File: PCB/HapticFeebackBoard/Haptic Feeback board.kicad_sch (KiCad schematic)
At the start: 3 parts, among them J1 Conn_01x02, J2 Conn_01x04, Q1 2N7002E

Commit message: Updated Haptic Feedback Board
Should be close to final schematic
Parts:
- removed J1: Conn_01x02, symbol Connector_Generic:Conn_01x02
- removed J2: Conn_01x04, symbol Connector_Generic:Conn_01x04
- added C1: 1uF, Capacitor_SMD:C_0805_2012Metric_Pad1.18x1.45mm_HandSolder, symbol Device:C_Small
- added H1, H2, H3, H4: MountingHole, MountingHole:MountingHole_3.2mm_M3, symbol Mechanical:MountingHole
- added J1: 1769, Adafruit Accessories JST-PH 2-pin SMT Right Angle Connect:1769, symbol 1769:1769
- added J2, J3, J4: Conn_01x02, Connector_Molex:Molex_KK-254_AE-6410-02A_1x02_P2.54mm_Vertical, symbol Connector_Generic:Conn_01x02
- added R1: 10k, Resistor_SMD:R_0805_2012Metric_Pad1.20x1.40mm_HandSolder, symbol Device:R
- added SW1: PTS526 SM15 SMTR2 LFS, PTS526 SM15 SMTR2 LFS:SON4_PTS526 SM15 SMTR2 LFS_CNK, symbol PTS526 SM15 SMTR2 LFS:PTS526_SM15_SMTR2_LFS
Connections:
- net BMS Power: now also J1.1, SW1.1, SW1.2
- net GND: now also C1.2, J1.2, J3.2 (Pin_2), J4.2 (Pin_2)
- net GPIO: now also Q1.1 (G), J2.2 (Pin_2)
- net Motor1: now reaches Q1.2 (S)
- net Motor1: now also J3.1 (Pin_1), J4.1 (Pin_1)
- new net: C1.1, R1.1, SW1.3, SW1.4
- new net MCU: J2.1 (Pin_1), R1.2

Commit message: Recovery attempt 2
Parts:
- removed C1: 1uF, Capacitor_SMD:C_0805_2012Metric_Pad1.18x1.45mm_HandSolder, symbol Device:C_Small
- removed H1, H2, H3, H4: MountingHole, MountingHole:MountingHole_3.2mm_M3, symbol Mechanical:MountingHole
- removed J1: 1769, Adafruit Accessories JST-PH 2-pin SMT Right Angle Connect:1769, symbol 1769:1769
- removed J2, J3, J4: Conn_01x02, Connector_Molex:Molex_KK-254_AE-6410-02A_1x02_P2.54mm_Vertical, symbol Connector_Generic:Conn_01x02
- removed R1: 10k, Resistor_SMD:R_0805_2012Metric_Pad1.20x1.40mm_HandSolder, symbol Device:R
- removed SW1: PTS526 SM15 SMTR2 LFS, PTS526 SM15 SMTR2 LFS:SON4_PTS526 SM15 SMTR2 LFS_CNK, symbol PTS526 SM15 SMTR2 LFS:PTS526_SM15_SMTR2_LFS
- added J1: Conn_01x02, symbol Connector_Generic:Conn_01x02
- added J2: Conn_01x04, symbol Connector_Generic:Conn_01x04
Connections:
- net BMS Power: now also J1.2 (Pin_2)
- net GND: now also J2.1 (Pin_1), J2.3 (Pin_3)
- net GPIO: no longer Q1.1 (G)
- net Motor1: no longer names the net of Q1.2 (S)
- net Motor1: now also J2.2 (Pin_2), J2.4 (Pin_4)
- new net: J1.1 (Pin_1), Q1.1 (G)
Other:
- company: (none) -> Running Cadence Measurement Belt
- title: (none) -> Haptic Feedback Board

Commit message: Updating Haptic Feedback Board
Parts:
- removed J1: Conn_01x02, symbol Connector_Generic:Conn_01x02
- removed J2: Conn_01x04, symbol Connector_Generic:Conn_01x04
- added C1: 1uF, Capacitor_SMD:C_0805_2012Metric_Pad1.18x1.45mm_HandSolder, symbol Device:C_Small
- added H1, H2, H3, H4: MountingHole, MountingHole:MountingHole_3.2mm_M3, symbol Mechanical:MountingHole
- added J1: 1769, Adafruit Accessories JST-PH 2-pin SMT Right Angle Connect:1769, symbol 1769:1769
- added J2, J3, J4: Conn_01x02, Connector_Molex:Molex_KK-254_AE-6410-02A_1x02_P2.54mm_Vertical, symbol Connector_Generic:Conn_01x02
- added R1: 10k, Resistor_SMD:R_0805_2012Metric_Pad1.20x1.40mm_HandSolder, symbol Device:R
- added SW1: PTS526 SM15 SMTR2 LFS, PTS526 SM15 SMTR2 LFS:SON4_PTS526 SM15 SMTR2 LFS_CNK, symbol PTS526 SM15 SMTR2 LFS:PTS526_SM15_SMTR2_LFS
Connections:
- net BMS Power: now also J1.1, SW1.1, SW1.2
- net GND: now also C1.2, J1.2, J3.2 (Pin_2), J4.2 (Pin_2)
- net GPIO: now also Q1.1 (G), J2.2 (Pin_2)
- net Motor1: now reaches Q1.2 (S)
- net Motor1: now also J3.1 (Pin_1), J4.1 (Pin_1)
- new net: C1.1, R1.1, SW1.3, SW1.4
- new net MCU: J2.1 (Pin_1), R1.2
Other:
- company: Running Cadence Measurement Belt -> (none)
- title: Haptic Feedback Board -> (none)

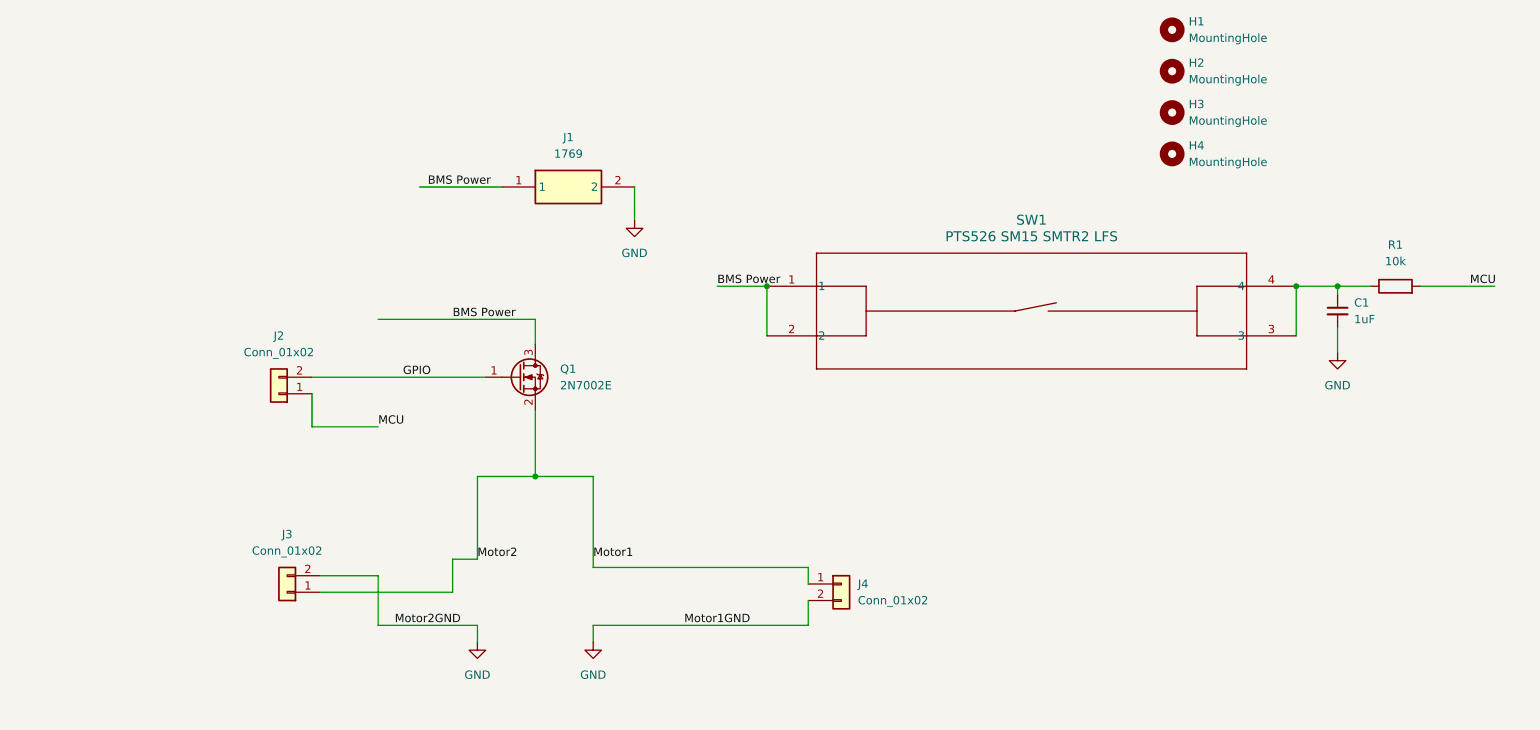
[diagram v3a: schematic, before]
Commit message: Further minor edits, added power LED
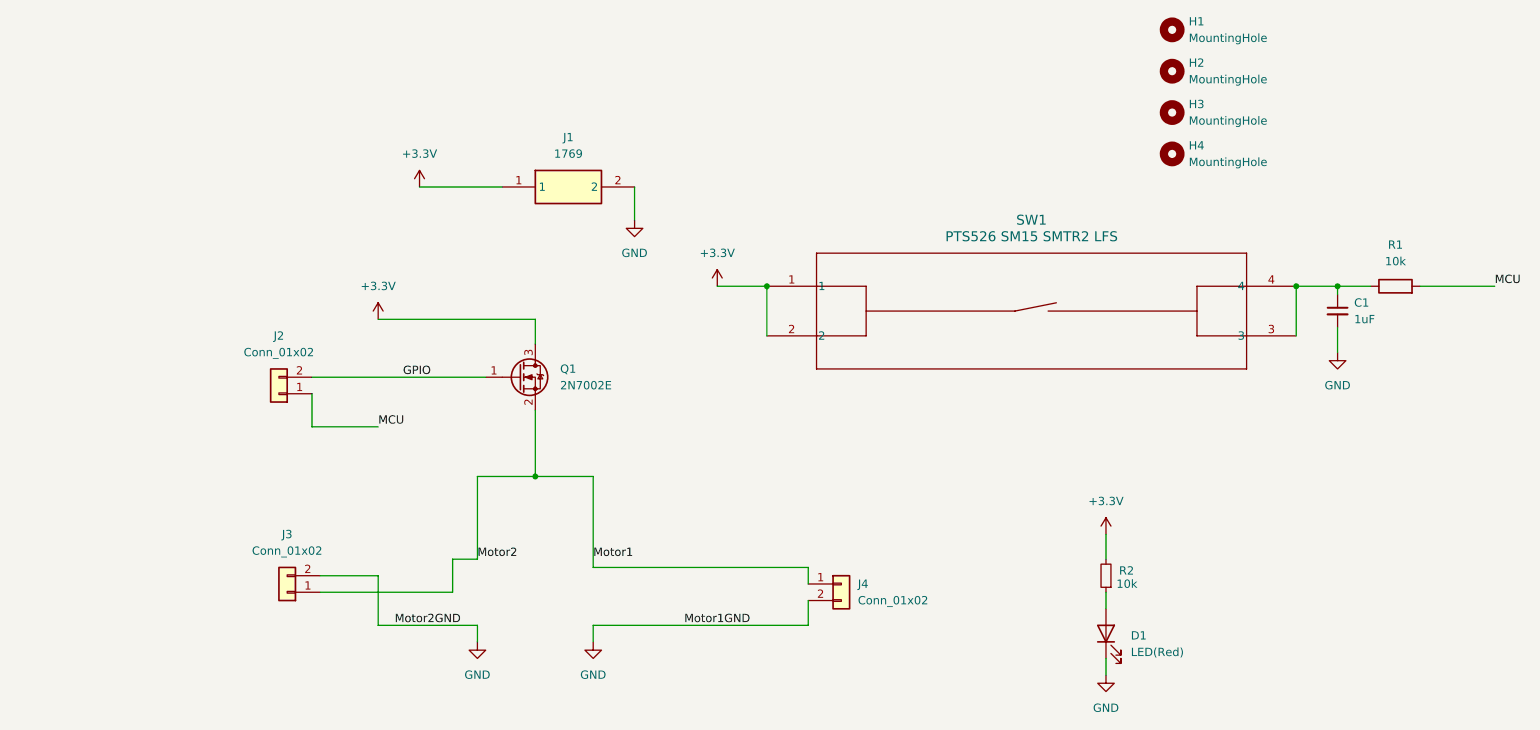
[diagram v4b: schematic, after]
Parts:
- added D1: LED(Red), LED_SMD:LED_0603_1608Metric_Pad1.05x0.95mm_HandSolder, symbol Device:LED
- added R2: 10k, Resistor_SMD:R_0805_2012Metric_Pad1.20x1.40mm_HandSolder, symbol Device:R_Small
- Q1: footprint Package_TO_SOT_SMD:SOT-23 -> Package_TO_SOT_SMD:SOT-23-3
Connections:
- net GND: now also D1.1 (K)
- net BMS Power renamed +3.3V
- net +3.3V: now also R2.2
- new net: D1.2 (A), R2.1

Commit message: Updated Haptic Feedback Board
Changed motor to be connected to the drain rather than source
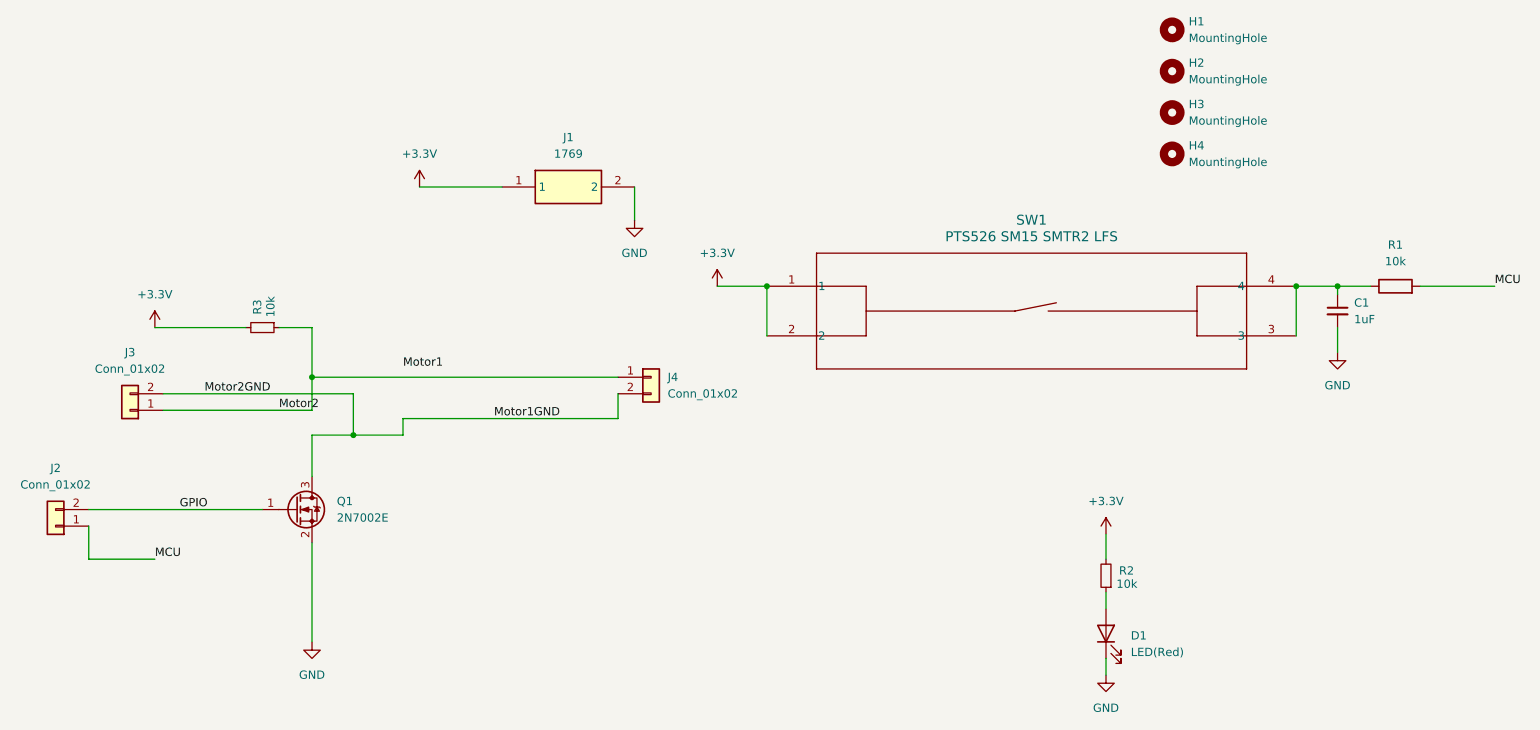
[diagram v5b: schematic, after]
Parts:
- added R3: 10k, Resistor_SMD:R_0805_2012Metric_Pad1.20x1.40mm_HandSolder, symbol Device:R_Small
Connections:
- net +3.3V: now also R3.2; no longer Q1.3 (D)
- net GND: now also Q1.2 (S); no longer J3.2 (Pin_2), J4.2 (Pin_2)
- net Motor1: no longer J3.1 (Pin_1), J4.1 (Pin_1), Q1.2 (S)
- new net Motor1GND: J3.2 (Pin_2), J4.2 (Pin_2), Q1.3 (D)
- new net Motor2: J3.1 (Pin_1), J4.1 (Pin_1), R3.1
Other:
- moved on the sheet: J2, J3, J4, Q1
